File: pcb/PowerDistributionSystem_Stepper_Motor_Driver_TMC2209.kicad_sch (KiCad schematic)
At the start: 13 parts, among them U4 TMC2209-LA-T

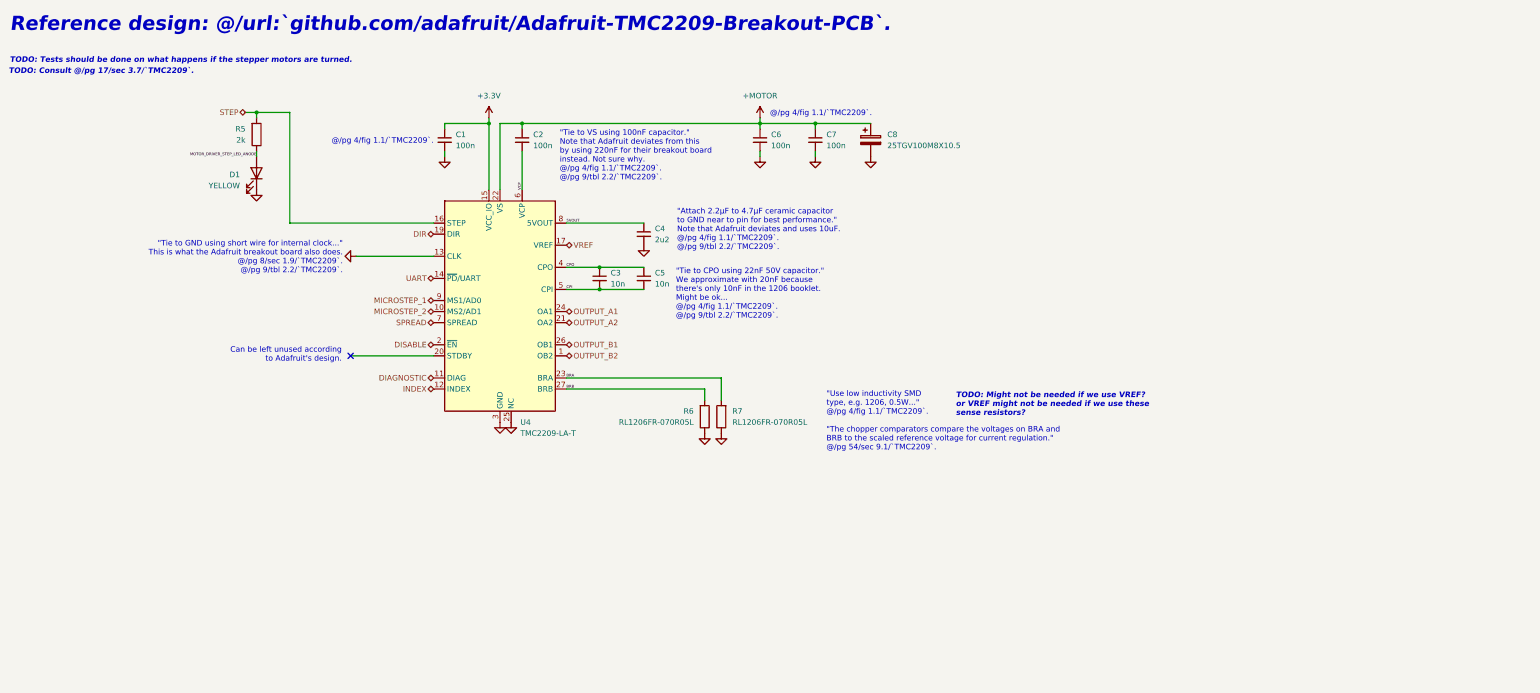
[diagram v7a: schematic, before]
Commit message: Revised TMC2209 schematic.
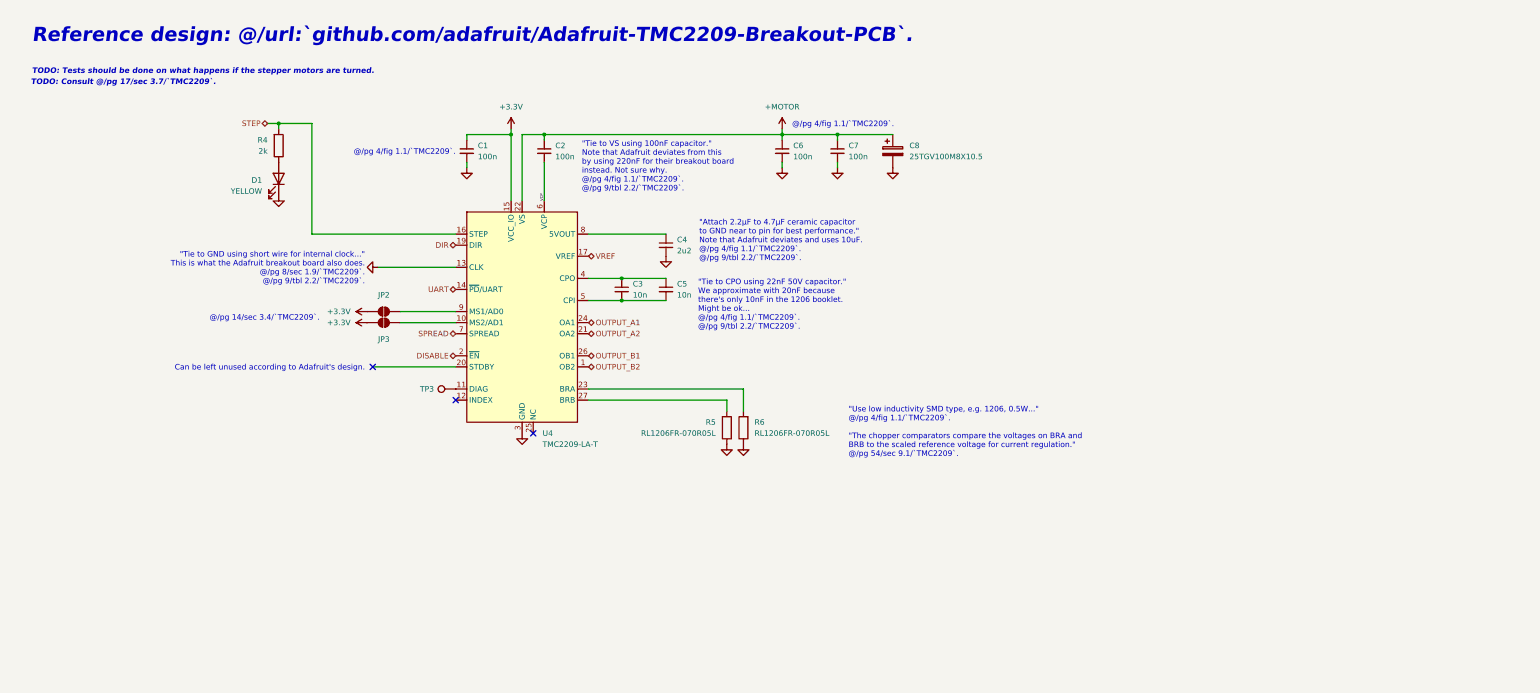
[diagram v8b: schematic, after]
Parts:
- added JP2, JP3: SolderJumper_2_Open, Jumper:SolderJumper-2_P1.3mm_Open_RoundedPad1.0x1.5mm, symbol Jumper:SolderJumper_2_Open
- added TP3: TestPoint, TestPoint:TestPoint_Pad_1.0x1.0mm, symbol Connector:TestPoint
- renumbered R5 to R4, R6 to R5, R7 to R6
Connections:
- net +3.3V: now also JP2.1 (A), JP3.1 (A)
- net GND: no longer U4.25 (NC)
- net 5VOUT: no longer names the net of C4.1, U4.8 (5VOUT)
- net BRA: no longer names the net of R6.2, U4.23 (BRA)
- net BRB: no longer names the net of R5.2, U4.27 (BRB)
- net CPI: no longer names the net of C3.2, C5.2, U4.5 (CPI)
- net CPO: no longer names the net of C3.1, C5.1, U4.4 (CPO)
- net DIAGNOSTIC: no longer names the net of U4.11 (DIAG)
- net DIAGNOSTIC: now also TP3.1
- net INDEX: no longer names the net of U4.12 (INDEX)
- net MICROSTEP_1: no longer names the net of U4.9 (MS1/AD0)
- net MICROSTEP_1: now also JP2.2 (B)
- net MICROSTEP_2: no longer names the net of U4.10 (MS2/AD1)
- net MICROSTEP_2: now also JP3.2 (B)
- net MOTOR_DRIVER_STEP_LED_ANODE: no longer names the net of D1.2 (A), R4.1
- no-connect marks 1 -> 3
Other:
- note added: "@/pg 14/sec 3.4/`TMC2209`."
- note removed: "TODO: Might not be needed if we use VREF? or VREF might not be needed if we use these sense resistors?"
- moved on the sheet: C1, C2, C3, C4, C5, C6, C7, C8, D1, R4, R5, R6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
